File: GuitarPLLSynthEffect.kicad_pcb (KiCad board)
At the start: 2 copper layers, 83.1 x 165.1 mm, 64 parts

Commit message: update
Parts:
- moved J_AUX2MAIN_VOL1 17.8 mm to (137.2, 88.9)
- moved J_AUX2MAIN_FXSW1 17.7 mm to (137.2, 71.1)
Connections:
- J_AUX2MAIN_INSW1 pad 4: (no net) -> Net-(J_AUX2MAIN_INSW1-Pad4)
- J_AUX2MAIN_LED1 pad 3: (no net) -> Net-(J_AUX2MAIN_LED1-Pad3)
- J_AUX2MAIN_LED1 pad 4: (no net) -> Net-(J_AUX2MAIN_LED1-Pad4)
- J_AUX2MAIN_VOL1 pad 4: (no net) -> Net-(J_AUX2MAIN_VOL1-Pad4)
- J_CLEAN_IN1 pad 3: (no net) -> Net-(J_CLEAN_IN1-Pad3)
- J_DIRTY_IN1 pad 3: (no net) -> Net-(J_DIRTY_IN1-Pad3)
- J_MAIN2AUX_INSW1 pad 4: (no net) -> Net-(J_MAIN2AUX_INSW1-Pad4)
- J_MAIN2AUX_LED1 pad 3: (no net) -> Net-(J_MAIN2AUX_LED1-Pad3)
- J_MAIN2AUX_LED1 pad 4: (no net) -> Net-(J_MAIN2AUX_LED1-Pad4)
- J_MAIN2AUX_VOL1 pad 4: (no net) -> Net-(J_MAIN2AUX_VOL1-Pad4)
- J_OU1 pad 2: (no net) -> Net-(J_OU1-Pad2)
- J_OU1 pad 3: (no net) -> Net-(J_OU1-Pad3)
- J_POWER1 pad 3: (no net) -> Net-(J_POWER1-Pad3)
- SW_BYPASS1 pad 7: (no net) -> Net-(SW_BYPASS1-Pad7)
- U_MAINOA1 pad 1: (no net) -> Net-(U_MAINOA1-Pad1)
- U_MAINOA1 pad 2: (no net) -> Net-(U_MAINOA1-Pad2)
- U_MAINOA1 pad 3: (no net) -> Net-(U_MAINOA1-Pad3)
- U_NEG1 pad 6: (no net) -> Net-(U_NEG1-Pad6)
- U_NEG1 pad 7: (no net) -> Net-(U_NEG1-Pad7)
- U_NEG2 pad 6: (no net) -> Net-(U_NEG2-Pad6)
- U_NEG2 pad 7: (no net) -> Net-(U_NEG2-Pad7)
- U_PLL1 pad 1: (no net) -> Net-(U_PLL1-Pad1)
- U_PLL1 pad 10: (no net) -> Net-(U_PLL1-Pad10)
- U_PLL1 pad 12: (no net) -> Net-(U_PLL1-Pad12)
- U_PLL1 pad 15: (no net) -> Net-(U_PLL1-Pad15)
- U_PLL1 pad 2: (no net) -> Net-(U_PLL1-Pad2)
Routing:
- net Net-(J_AUX2MAIN_FXSW1-Pad4): track 8.82 -> 61.7 mm
- net Net-(J_AUX2MAIN_FXSW1-Pad5): track 14.0 -> 52.7 mm
- net Net-(J_AUX2MAIN_VOL1-Pad2): track 11.5 -> 32.1 mm
- net Net-(J_AUX2MAIN_VOL1-Pad3): track 8.20 -> 27.0 mm
- net Net-(J_AUX2MAIN_FXSW1-Pad3): track 49.5 -> 68.1 mm
- net Net-(J_AUX2MAIN_FXSW1-Pad2): track 44.4 -> 60.8 mm
- net Net-(J_AUX2MAIN_FXSW1-Pad1): track 39.3 -> 52.0 mm
- net Net-(FXVOL1-Pad1): track 43.9 -> 53.1 mm
- net Net-(FXVOL1-Pad3): track 36.9 -> 45.1 mm
- net Net-(J_AUX2MAIN_VOL1-Pad1): track 16.2 -> 20.1 mm
- net Net-(J_AUX2MAIN_FXSW1-Pad6): track 19.2 -> 22.4 mm
- net /GND: track 27.6 -> 25.8 mm
- net /9V: track 267.4 -> 269.2 mm
- net /INSW_P3: track 46.6 -> 46.1 mm

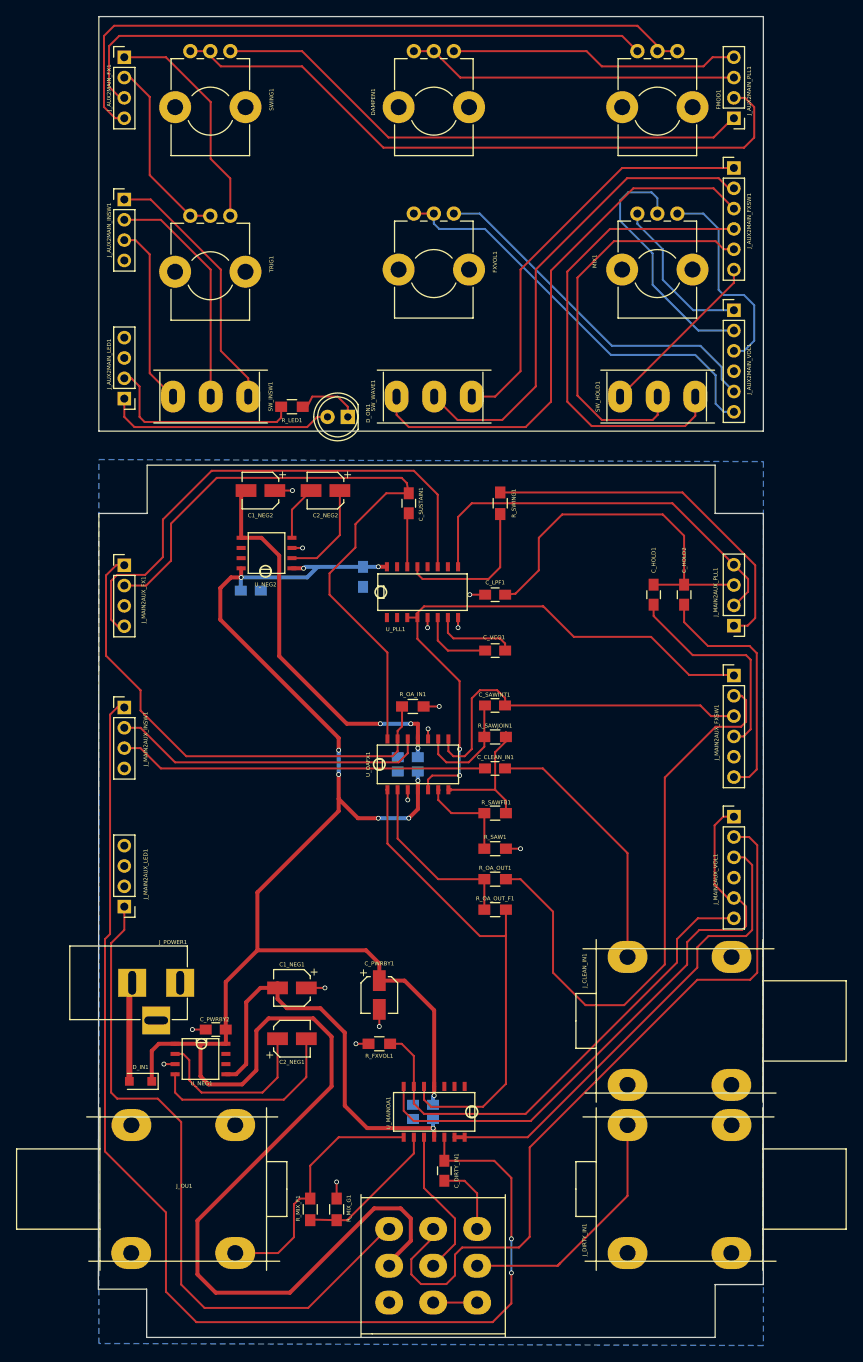
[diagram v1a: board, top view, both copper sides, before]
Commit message: Board Layout updates
- Increased PLL footprint width
- Separated FX TL074 into 2 TL072's.
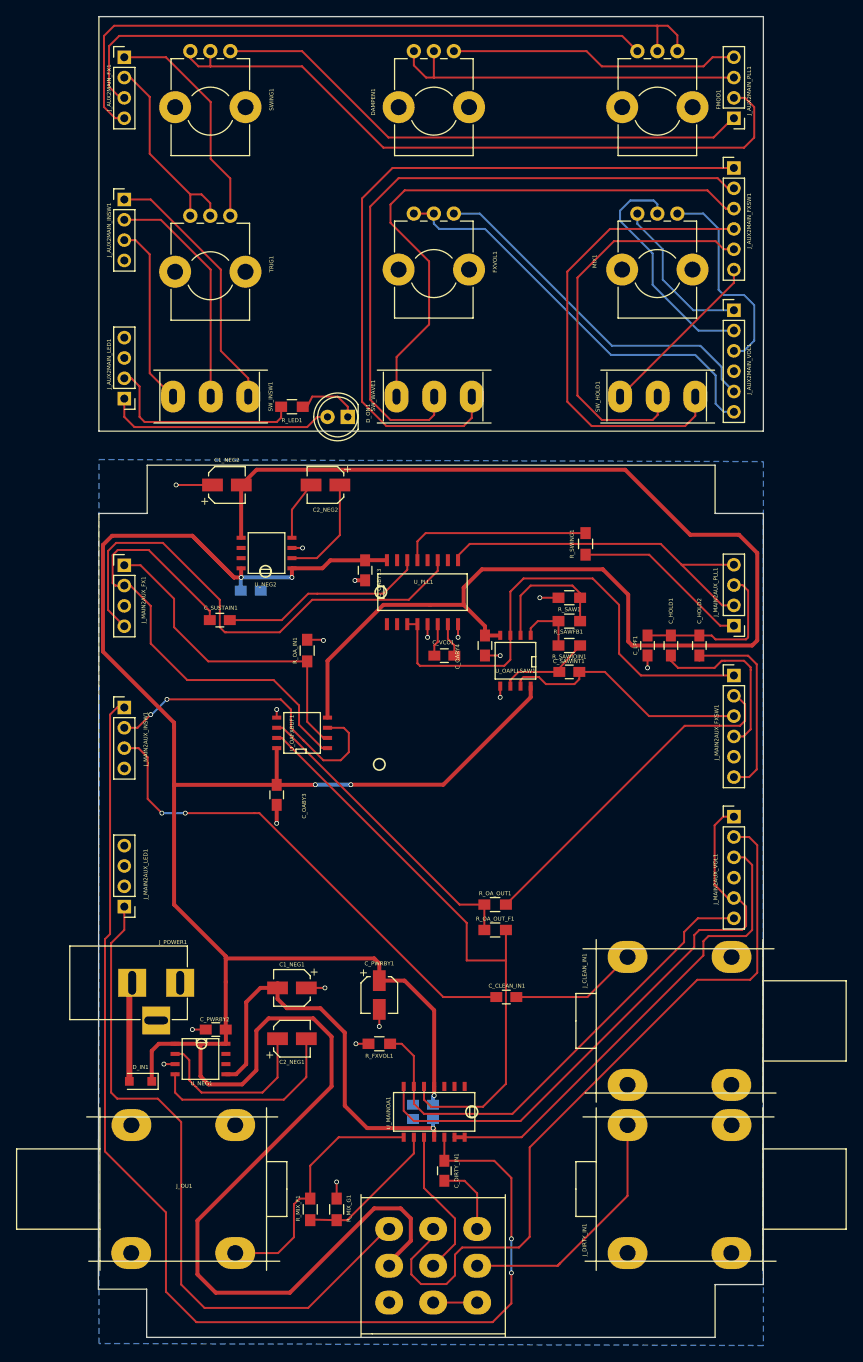
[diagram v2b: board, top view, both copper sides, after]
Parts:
- removed U_OAFX1: TL074, SMD_Packages:SOIC-14_N
- added U_OAFXBUF1: TL072, SMD_Packages:SOIC-8-N, F.Cu at (83.2, 141.7)
- added U_OAPLLSAW1: TL072, SMD_Packages:SOIC-8-N, F.Cu at (109.9, 132.7)
- C_OABY13, C_OABY3, C_OABY4: moved to F.Cu
- U_PLL1: footprint SMD_Packages:SO-16-N -> Custom_SMD_Packages:SO-16-N++
- moved R_SAW1 32.7 mm to (116.6, 124.8), turned to 180 degrees
- moved C_CLEAN_IN1 28.6 mm to (108.7, 174.8)
- moved C_SUSTAIN1 27.8 mm to (72.9, 127.6), turned to 0 degrees
- moved R_SAWFB1 25.7 mm to (116.6, 127.8), turned to 0 degrees
- moved C_LPF1 20.1 mm to (126.4, 130.8), turned to 270 degrees
- moved C_OABY4 17.0 mm to (106.0, 130.8), turned to 270 degrees
- moved C_OABY3 16.6 mm to (80.0, 149.5), turned to 270 degrees
- moved R_OA_IN1 14.9 mm to (83.8, 131.4), turned to 270 degrees
- moved R_SAWJOIN1 14.7 mm to (116.6, 130.8), turned to 180 degrees
- moved R_SWING1 11.8 mm to (118.6, 118.1), turned to 90 degrees
- moved C_SAWINT1 10.2 mm to (116.6, 134.1)
- moved C_HOLD1 6.71 mm to (129.3, 130.8)
- moved C_HOLD2 6.63 mm to (132.8, 130.8)
- moved C_VCO1 6.38 mm to (101.0, 132.1)
- moved C1_NEG2 4.25 mm to (73.8, 110.7), turned to 0 degrees
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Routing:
- net /Sheet5AC1BF71/-9V: track 50.1 -> 169.7 mm, vias 3 -> 0
- net /9V: track 269.2 -> 333.3 mm, vias 9 -> 5
- net Net-(J_AUX2MAIN_FXSW1-Pad1): track 52.0 -> 91.5 mm
- net /Sheet5AC1BF71/WAVESEL_P2: track 73.8 -> 43.3 mm
- net /Sheet5AC1BF71/DAMP_P1_2: track 47.1 -> 21.0 mm
- net /Sheet5AC1BF71/TRIG_P1_2: track 84.8 -> 60.9 mm
- net Net-(J_AUX2MAIN_FXSW1-Pad2): track 60.8 -> 84.3 mm
- net /Sheet5AC1BF71/SWING_P3: track 45.5 -> 22.4 mm
- net /Sheet5AC1BF71/TRIG_P3: track 62.4 -> 41.2 mm
- net Net-(C_SUSTAIN1-Pad2): track 6.77 -> 26.1 mm
- net Net-(C_CLEAN_IN1-Pad1): track 33.6 -> 16.9 mm
- net /INSW_P3: track 46.1 -> 62.4 mm, vias 0 -> 2
- net Net-(R_OA_OUT1-Pad1): track 22.9 -> 38.3 mm
- net /Sheet5AC1BF71/WAVESEL_P3: track 47.2 -> 32.0 mm
- net /Sheet5AC1BF71/SIG_OUT: track 62.3 -> 76.2 mm
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
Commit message: Board Layout redesign
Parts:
- added JTP1: TEST_1P, Measurement_Points:Measurement_Point_Round-SMD-Pad_Small, F.Cu at (108.1, 111.5)
- C_OABY1, C_OABY2, C_PWRBY3: moved to F.Cu
- moved R_SAW1 39.1 mm to (87.6, 151.1)
- moved R_SAWFB1 35.3 mm to (87.6, 148.0)
- moved C_OABY3 31.1 mm to (108.6, 137.2), turned to 0 degrees
- moved R_SAWJOIN1 28.7 mm to (102.2, 155.7)
- moved R_OA_OUT_F1 25.8 mm to (111.8, 141.0), turned to 270 degrees
- moved R_OA_OUT1 23.3 mm to (114.3, 141.0), turned to 90 degrees
- moved U_NEG1 22.3 mm to (90.2, 172.1)
- moved C_OABY4 22.2 mm to (95.9, 150.5), turned to 180 degrees
- moved C_OABY2 21.9 mm to (114.3, 175.0), turned to 0 degrees
- moved C1_NEG1 19.3 mm to (97.2, 185.4), turned to 90 degrees
- moved U_OAFXBUF1 19.2 mm to (102.2, 139.1), turned to 270 degrees
- moved C1_NEG2 19.0 mm to (92.7, 112.4), turned to 180 degrees
- moved C_OABY13 18.8 mm to (109.9, 121.9), turned to 0 degrees
- moved U_OAPLLSAW1 17.6 mm to (102.2, 148.6), turned to 270 degrees
- moved C2_NEG2 17.0 mm to (69.2, 112.4)
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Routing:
- net /Sheet5AC1BF71/-9V: track 169.7 -> 64.6 mm, vias 0 -> 3
- net /9V: track 333.3 -> 243.7 mm, vias 5 -> 10
- net /INSW_P1: track 151.3 -> 111.5 mm, vias 2 -> 0
- net Net-(R_SAWFB1-Pad1): track 8.48 -> 43.5 mm
- net Net-(J_OU1-Pad1): track 31.9 -> 63.9 mm
- net Net-(R_OA_OUT1-Pad1): track 38.3 -> 9.98 mm
- net /Sheet5AC1BF71/FMOD_P2_P3: track 63.0 -> 89.5 mm
- net Net-(C_SUSTAIN1-Pad2): track 26.1 -> 50.3 mm
- net Net-(SW_BYPASS1-Pad5): track 19.2 -> 40.9 mm
- net Net-(R_MIX_F1-Pad2): track 18.5 -> 38.9 mm
- net /Sheet5AC1BF71/SIG_OUT: track 76.2 -> 95.7 mm
- net /Sheet5AC1BF71/WAVESEL_P2: track 43.3 -> 24.2 mm
- net /-9V: track 52.2 -> 34.5 mm, vias 1 -> 4
- net Net-(JTP1-Pad1): track 0.00 -> 17.4 mm, vias 0 -> 2
- net /MIX_P2: track 95.5 -> 111.5 mm
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
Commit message: Layout updates
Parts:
- added R_SFOUT1: 100K, Resistors_SMD:R_0805_HandSoldering, F.Cu at (120.7, 124.5)
- moved C_LPF1 15.9 mm to (120.7, 121.9), turned to 180 degrees
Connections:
- J_AUX2MAIN_INSW1 pad 4: Net-(J_AUX2MAIN_INSW1-Pad4) -> (no net)
- J_AUX2MAIN_LED1 pad 3: Net-(J_AUX2MAIN_LED1-Pad3) -> (no net)
- J_AUX2MAIN_LED1 pad 4: Net-(J_AUX2MAIN_LED1-Pad4) -> (no net)
- J_AUX2MAIN_VOL1 pad 4: Net-(J_AUX2MAIN_VOL1-Pad4) -> (no net)
- J_CLEAN_IN1 pad 3: Net-(J_CLEAN_IN1-Pad3) -> (no net)
- J_DIRTY_IN1 pad 3: Net-(J_DIRTY_IN1-Pad3) -> (no net)
- J_MAIN2AUX_INSW1 pad 4: Net-(J_MAIN2AUX_INSW1-Pad4) -> (no net)
- J_MAIN2AUX_LED1 pad 3: Net-(J_MAIN2AUX_LED1-Pad3) -> (no net)
- J_MAIN2AUX_LED1 pad 4: Net-(J_MAIN2AUX_LED1-Pad4) -> (no net)
- J_MAIN2AUX_VOL1 pad 4: Net-(J_MAIN2AUX_VOL1-Pad4) -> (no net)
- J_OU1 pad 2: Net-(J_OU1-Pad2) -> (no net)
- J_OU1 pad 3: Net-(J_OU1-Pad3) -> (no net)
- J_POWER1 pad 3: Net-(J_POWER1-Pad3) -> (no net)
- SW_BYPASS1 pad 7: Net-(SW_BYPASS1-Pad7) -> (no net)
- U_MAINOA1 pad 1: Net-(U_MAINOA1-Pad1) -> (no net)
- U_MAINOA1 pad 2: Net-(U_MAINOA1-Pad2) -> (no net)
- U_MAINOA1 pad 3: Net-(U_MAINOA1-Pad3) -> (no net)
- U_NEG1 pad 6: Net-(U_NEG1-Pad6) -> (no net)
- U_NEG1 pad 7: Net-(U_NEG1-Pad7) -> (no net)
- U_NEG2 pad 6: Net-(U_NEG2-Pad6) -> (no net)
- U_NEG2 pad 7: Net-(U_NEG2-Pad7) -> (no net)
- U_PLL1 pad 12: Net-(U_PLL1-Pad12) -> (no net)
- U_PLL1 pad 15: Net-(U_PLL1-Pad15) -> /9V
- U_PLL1 pad 2: Net-(U_PLL1-Pad2) -> (no net)
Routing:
- net /Sheet5AC1BF71/DAMP_P1_2: track 27.7 -> 48.1 mm
- net Net-(R_SFOUT1-Pad1): track 0.00 -> 18.9 mm
- net /GND: track 38.1 -> 40.4 mm, vias 20 -> 21
- net /9V: track 243.7 -> 245.0 mm
